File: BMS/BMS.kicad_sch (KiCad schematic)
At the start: 10 parts, among them U1 ATmega406-1AA

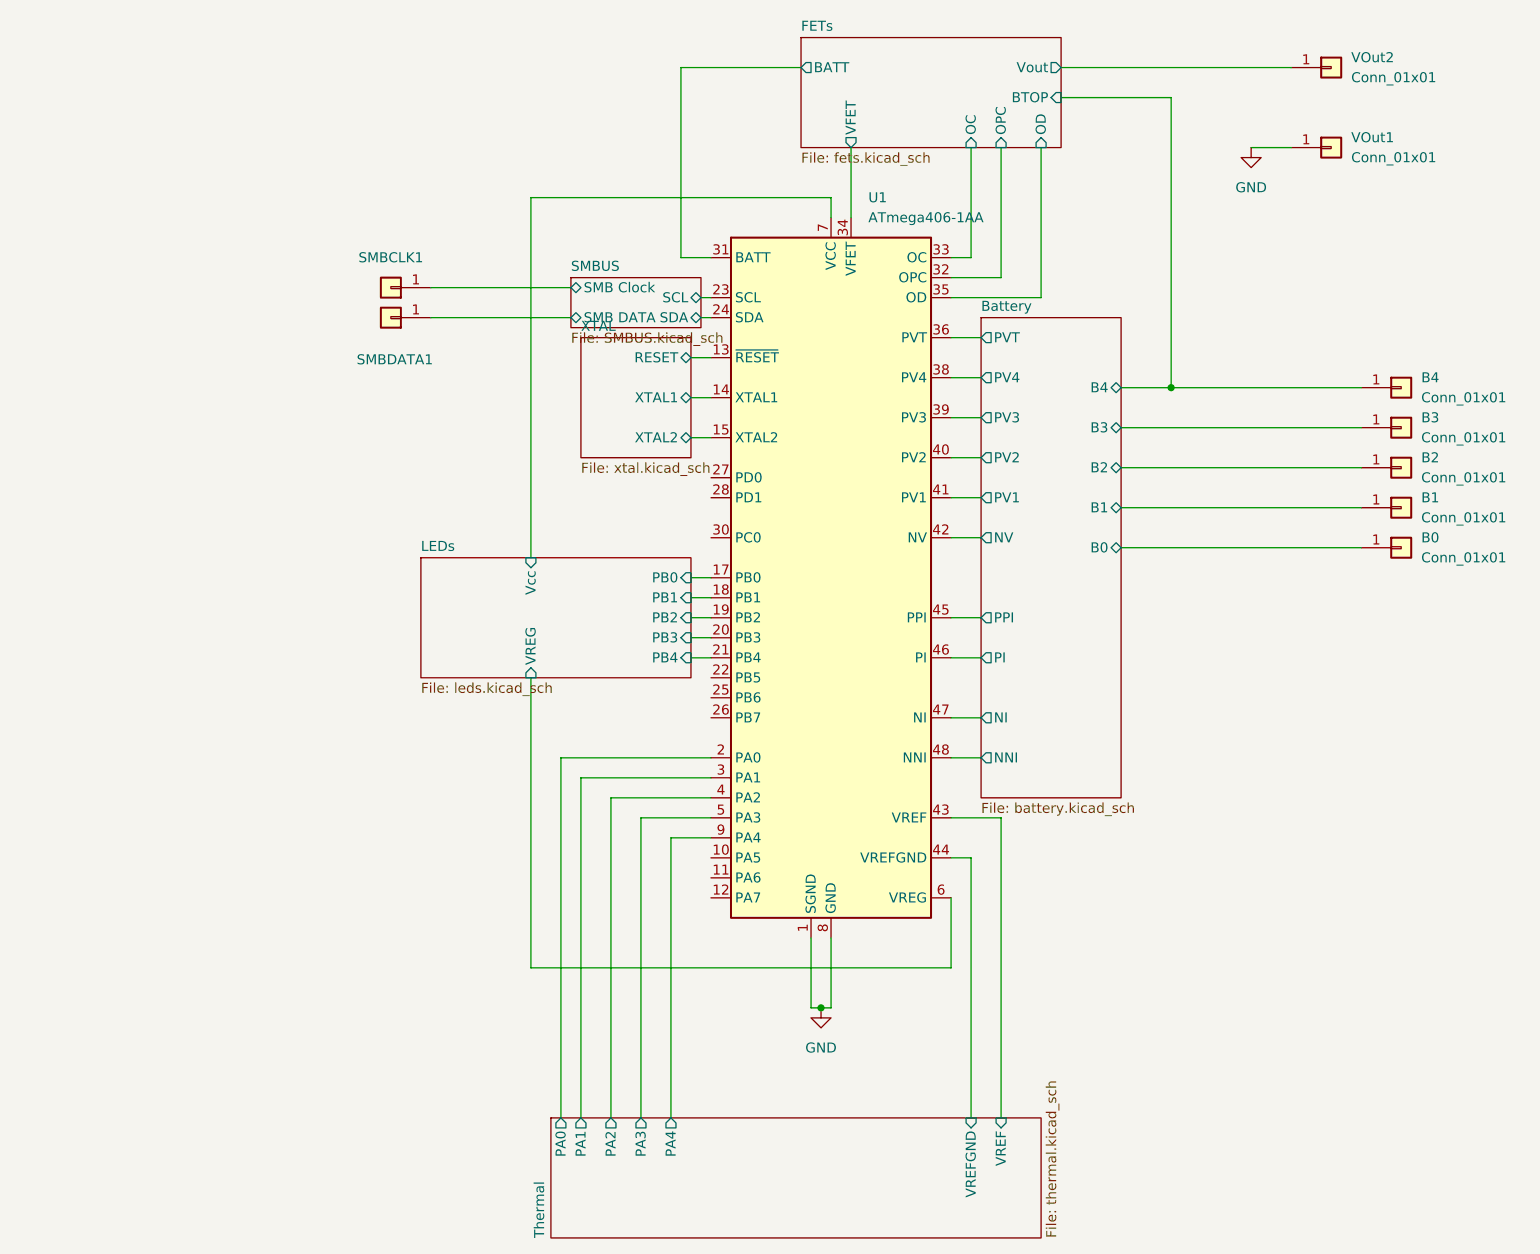
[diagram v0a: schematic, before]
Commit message: DCDC fix unavailable parts, BMS redesign, handle fix, rearrange top half
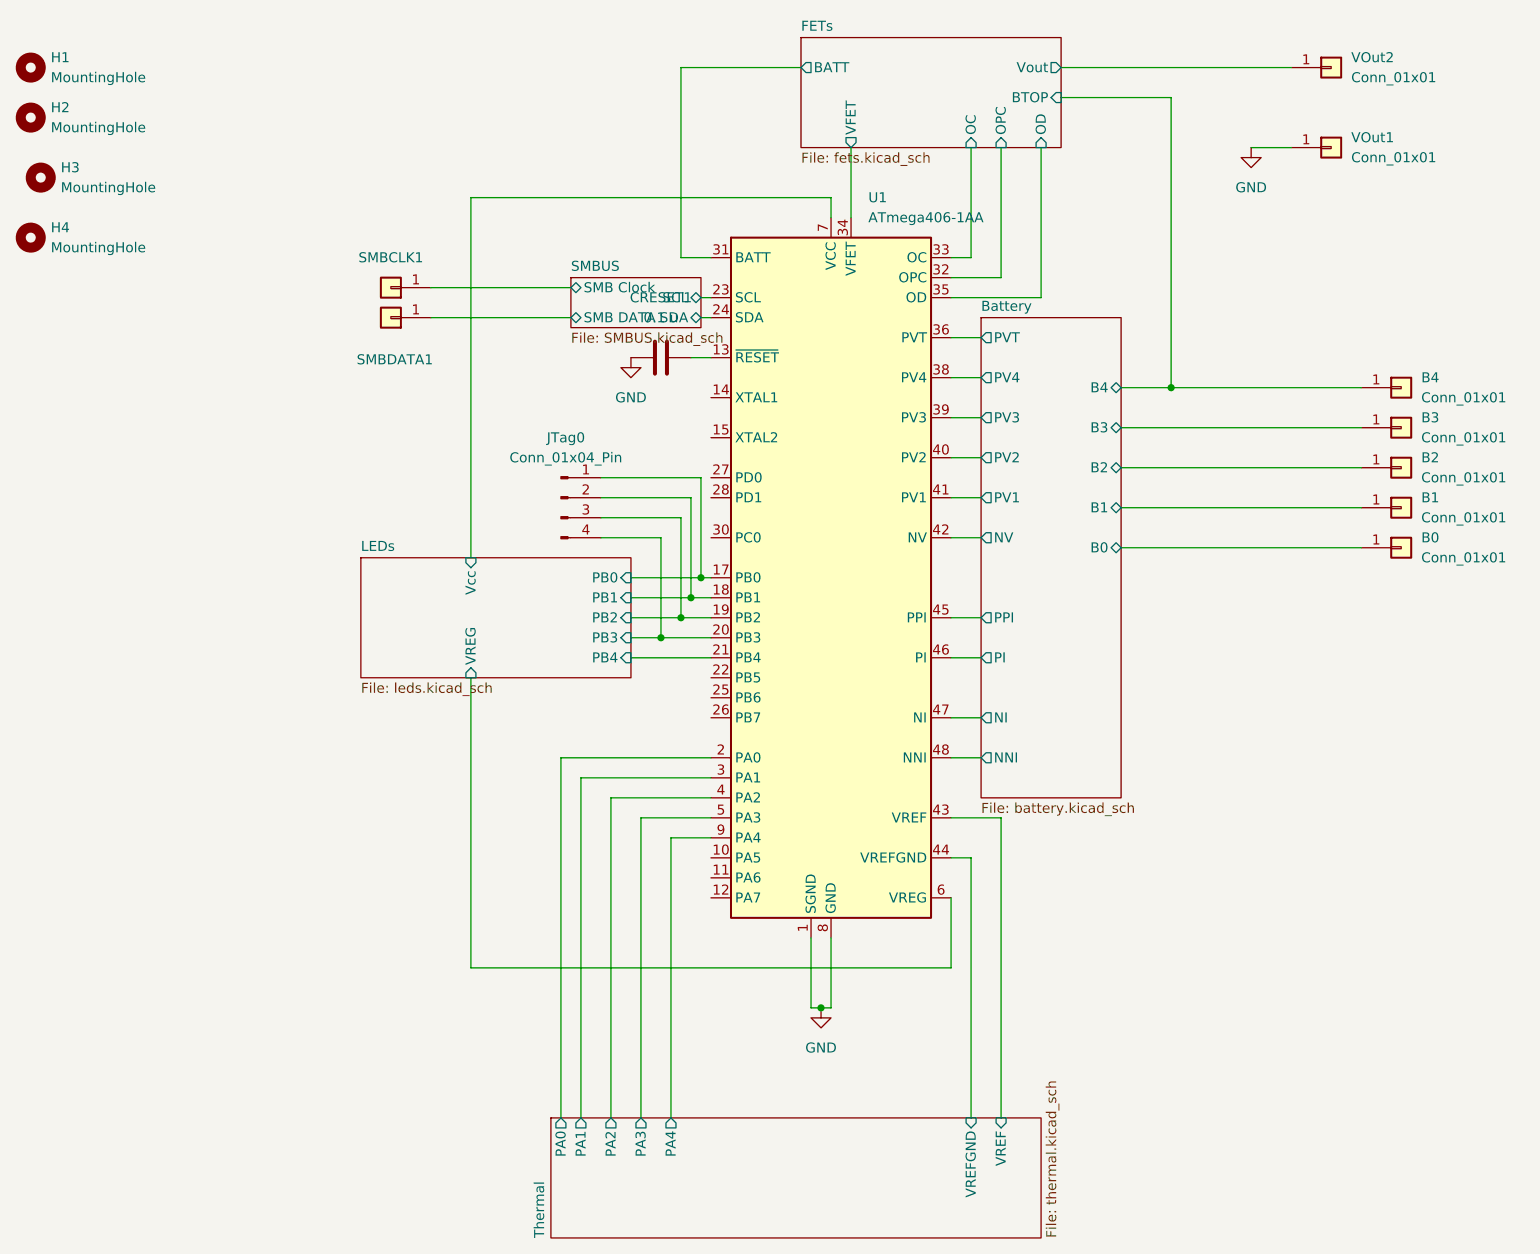
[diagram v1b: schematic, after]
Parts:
- added CRESET1: 0.1 u, Capacitor_SMD:C_0603_1608Metric, symbol Device:C
- added H1, H2, H3, H4: MountingHole, MountingHole:MountingHole_2.2mm_M2, symbol Mechanical:MountingHole
- added JTag0: Conn_01x04_Pin, Connector_PinHeader_2.00mm:PinHeader_1x04_P2.00mm_Horizontal, symbol Connector:Conn_01x04_Pin
- B0, B1, B2, B3, B4, SMBCLK1, SMBDATA1, VOut1, VOut2: now left out of the parts list
- U1: Manufacturer_Part_Number (none) -> ATmega406-1AA
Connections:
- net GND: now also CRESET1.1
- net LEDs/PB0: now also JTag0.1 (Pin_1)
- net LEDs/PB1: now also JTag0.2 (Pin_2)
- net LEDs/PB2: now also JTag0.3 (Pin_3)
- net LEDs/PB3: now also JTag0.4 (Pin_4)
- net XTAL/RESET: no longer names the net of U1.13 (~{RESET})
- net XTAL/RESET: now also CRESET1.2
- net XTAL/XTAL1: no longer names the net of U1.14 (XTAL1)
- net XTAL/XTAL2: no longer names the net of U1.15 (XTAL2)
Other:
- removed sheet XTAL
